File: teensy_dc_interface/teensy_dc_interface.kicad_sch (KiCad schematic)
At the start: 7 parts, among them J1 PJ301M-12, J2 PJ301M-12, J3 PJ301M-12, J4 PJ301M-12, U1 AK4458VN, U2 DEV-15583

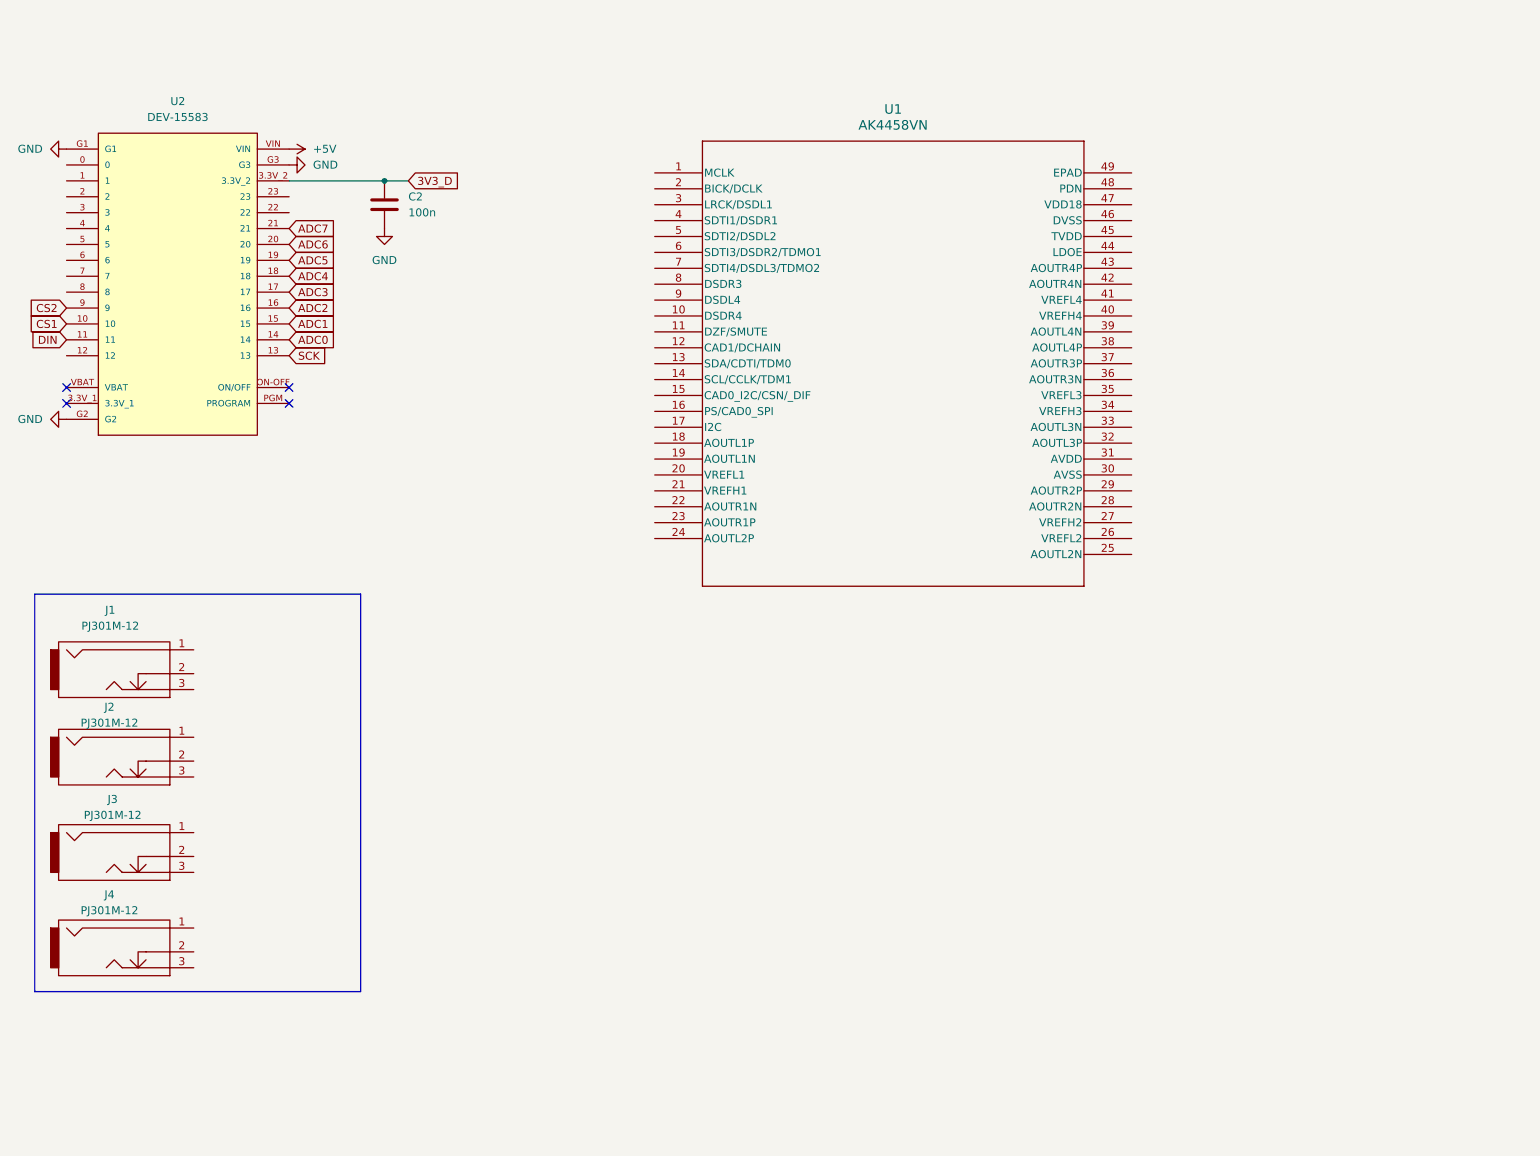
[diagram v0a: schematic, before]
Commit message: teensy interface prototype
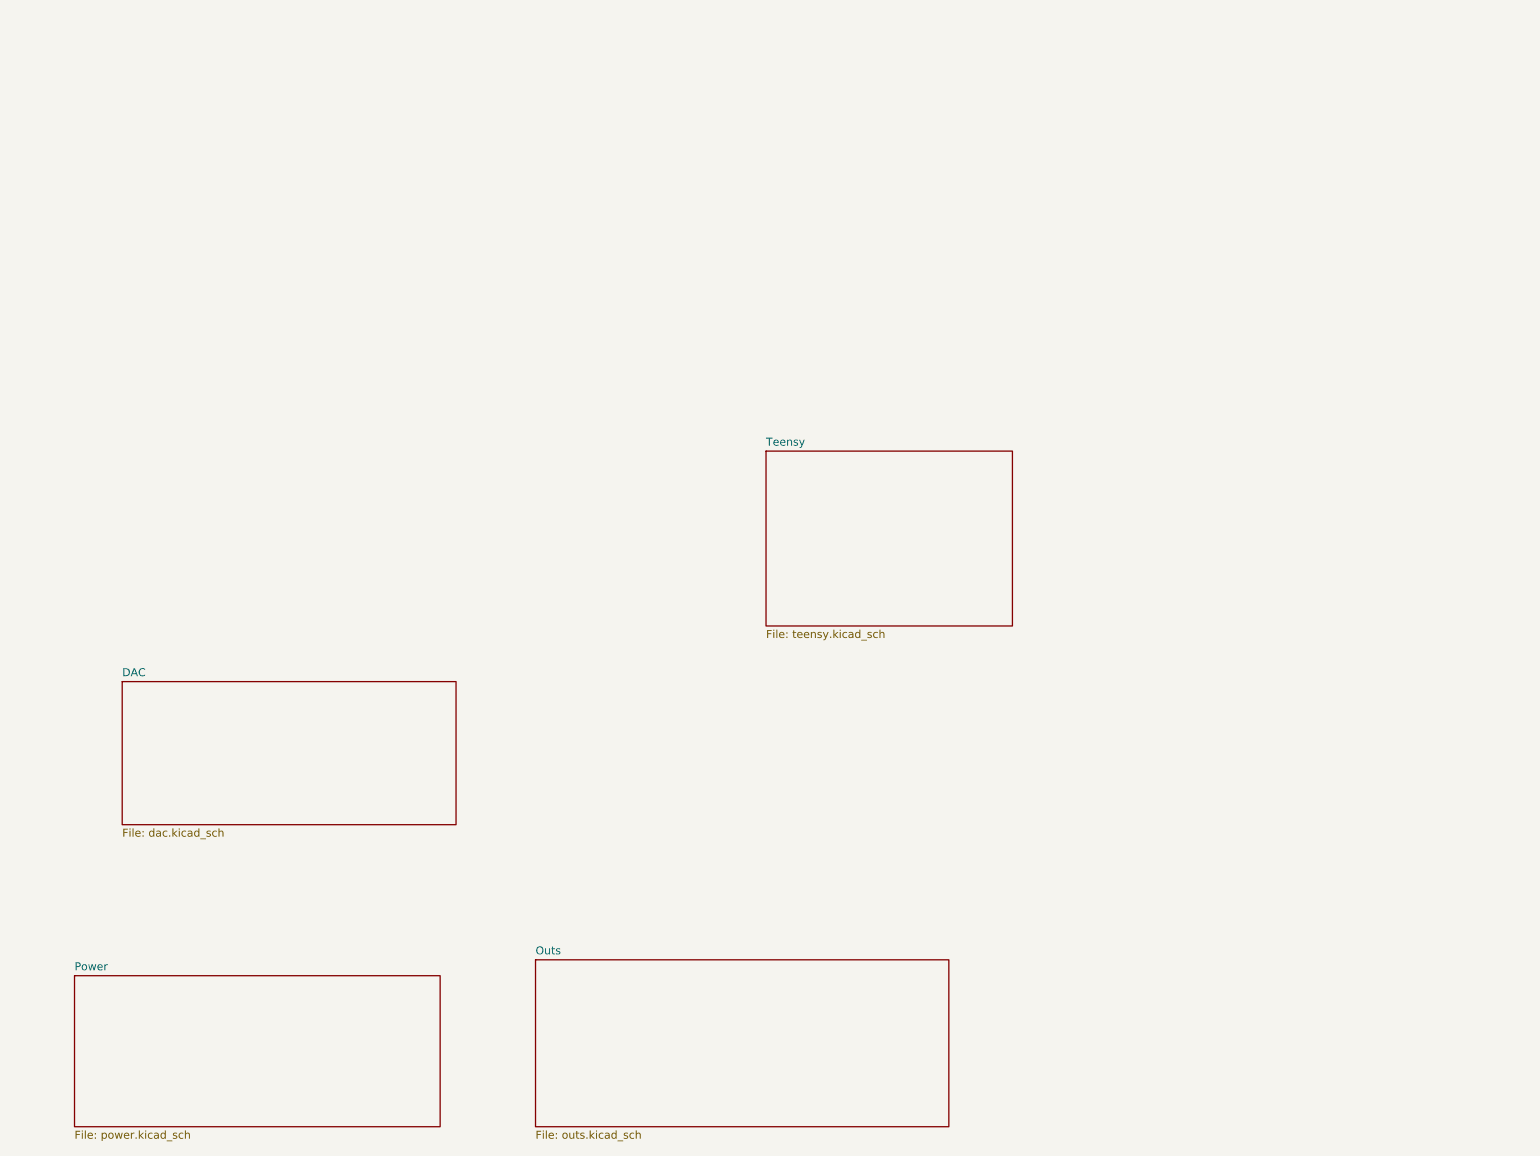
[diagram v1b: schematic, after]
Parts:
- removed C2: 100n, symbol Device:C
- removed J1, J2, J3, J4: PJ301M-12, symbol eurocad:PJ301M-12
- removed U1: AK4458VN, QFN48_7x7-0p5_AKM, symbol AK4458VN:AK4458VN
- removed U2: DEV-15583, DEV-15583:MODULE_DEV-15583, symbol Teensy4p0:DEV-15583
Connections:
- no-connect marks 4 -> 0
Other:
- added sheet DAC (dac.kicad_sch)
- added sheet Outs (outs.kicad_sch)
- added sheet Power (power.kicad_sch)
- added sheet Teensy (teensy.kicad_sch)

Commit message: teensy to dac connections
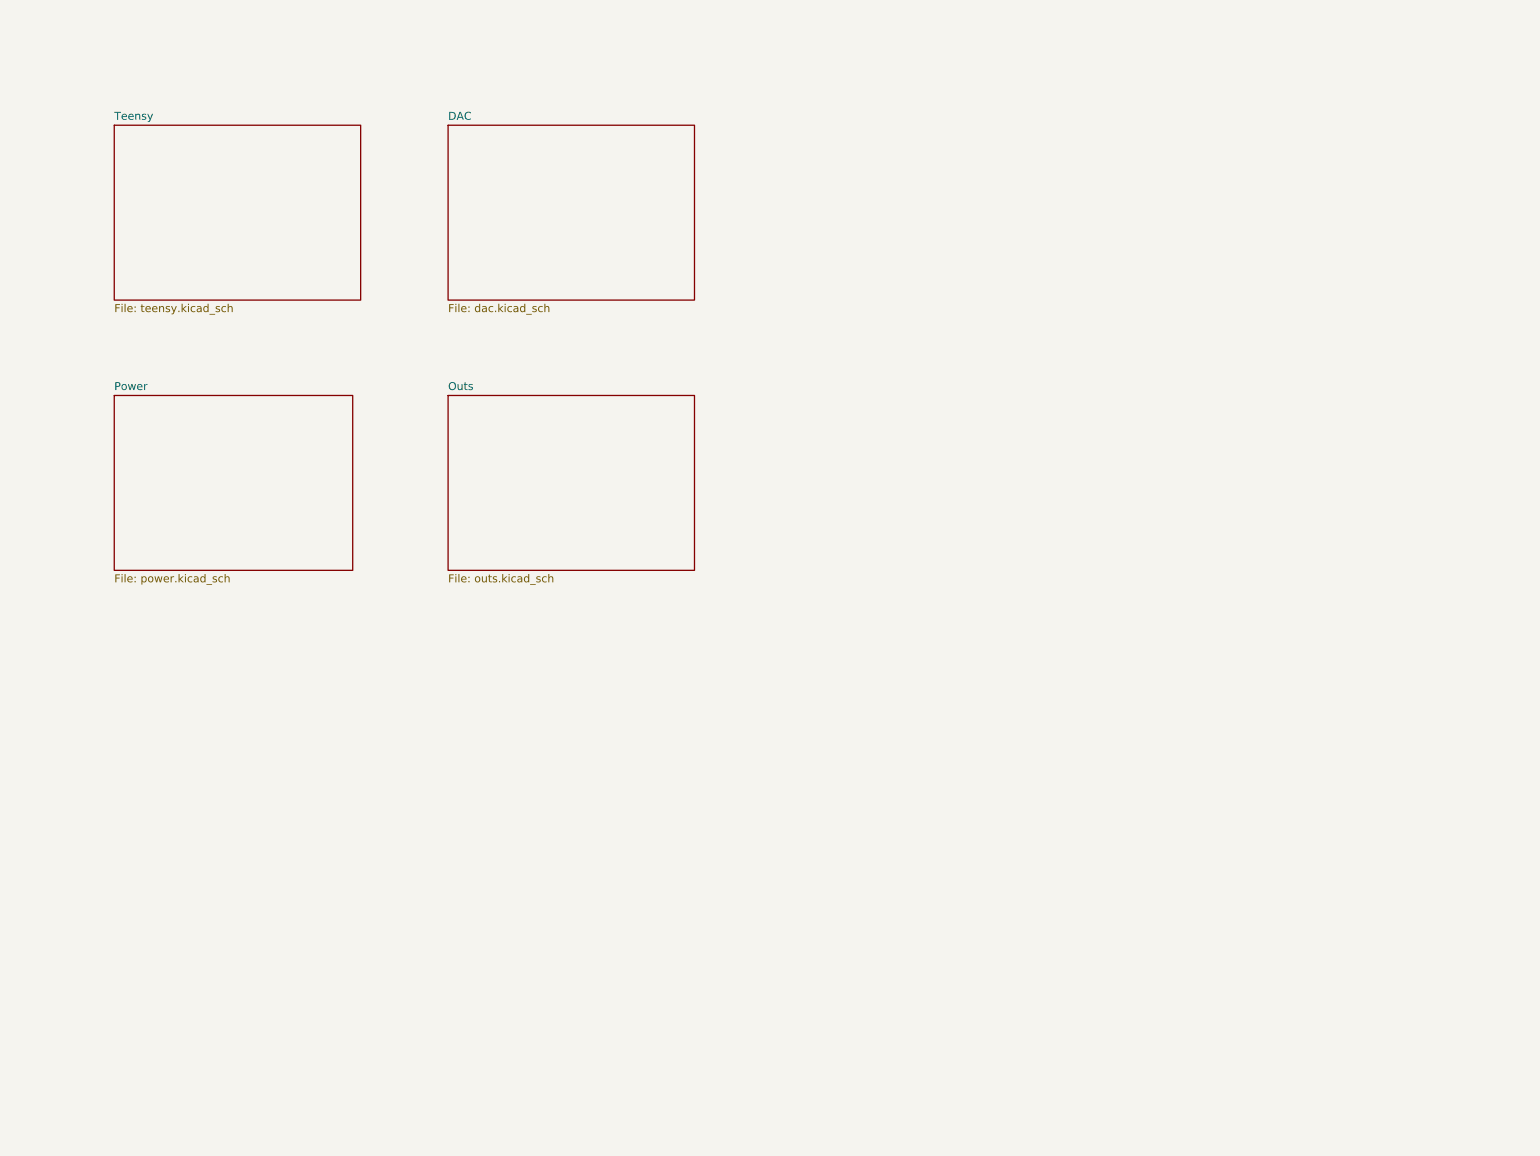
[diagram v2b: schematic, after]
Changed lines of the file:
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@@
 	(paper "A4")
 	(sheet
-		(at 20.32 166.37)
-		(size 58.42 24.13)
+		(at 26.67 73.66)
+		(size 38.1 27.94)
 		(fields_autoplaced yes)
 		(stroke
@@
 		)
 		(property "Sheetname" "Power"
-			(at 20.32 165.6584 0)
+			(at 26.67 72.9484 0)
 			(effects
 				(font
@@
 		)
 		(property "Sheetfile" "power.kicad_sch"
-			(at 20.32 191.0846 0)
+			(at 26.67 102.1846 0)
 			(effects
 				(font
@@
 	)
 	(sheet
-		(at 93.98 163.83)
-		(size 66.04 26.67)
+		(at 80.01 73.66)
+		(size 39.37 27.94)
 		(fields_autoplaced yes)
 		(stroke
@@
 		)
 		(property "Sheetname" "Outs"
-			(at 93.98 163.1184 0)
+			(at 80.01 72.9484 0)
 			(effects
 				(font
@@
 		)
 		(property "Sheetfile" "outs.kicad_sch"
-			(at 93.98 191.0846 0)
+			(at 80.01 102.1846 0)
 			(effects
 				(font
@@
 	)
 	(sheet
-		(at 27.94 119.38)
-		(size 53.34 22.86)
+		(at 80.01 30.48)
+		(size 39.37 27.94)
 		(fields_autoplaced yes)
 		(stroke
@@
 		)
 		(property "Sheetname" "DAC"
-			(at 27.94 118.6684 0)
+			(at 80.01 29.7684 0)
 			(effects
 				(font
@@
 		)
 		(property "Sheetfile" "dac.kicad_sch"
-			(at 27.94 142.8246 0)
+			(at 80.01 59.0046 0)
 			(effects
 				(font
@@
 	)
 	(sheet
-		(at 130.81 82.55)
+		(at 26.67 30.48)
 		(size 39.37 27.94)
 		(fields_autoplaced yes)
@@
 		)
 		(property "Sheetname" "Teensy"
-			(at 130.81 81.8384 0)
+			(at 26.67 29.7684 0)
 			(effects
 				(font
@@
 		)
 		(property "Sheetfile" "teensy.kicad_sch"
-			(at 130.81 111.0746 0)
+			(at 26.67 59.0046 0)
 			(effects
 				(font

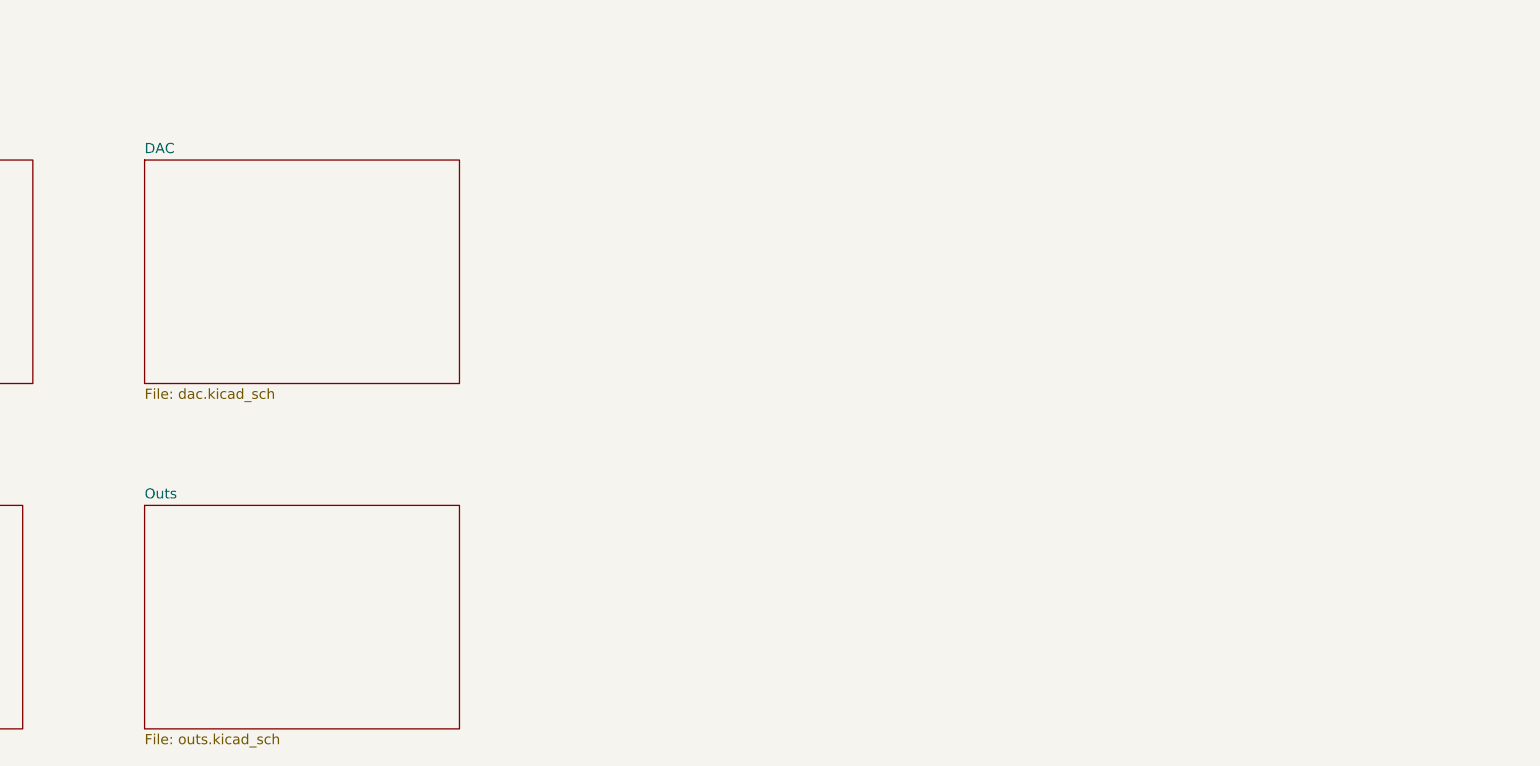
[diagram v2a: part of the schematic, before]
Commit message: out pairs as pages
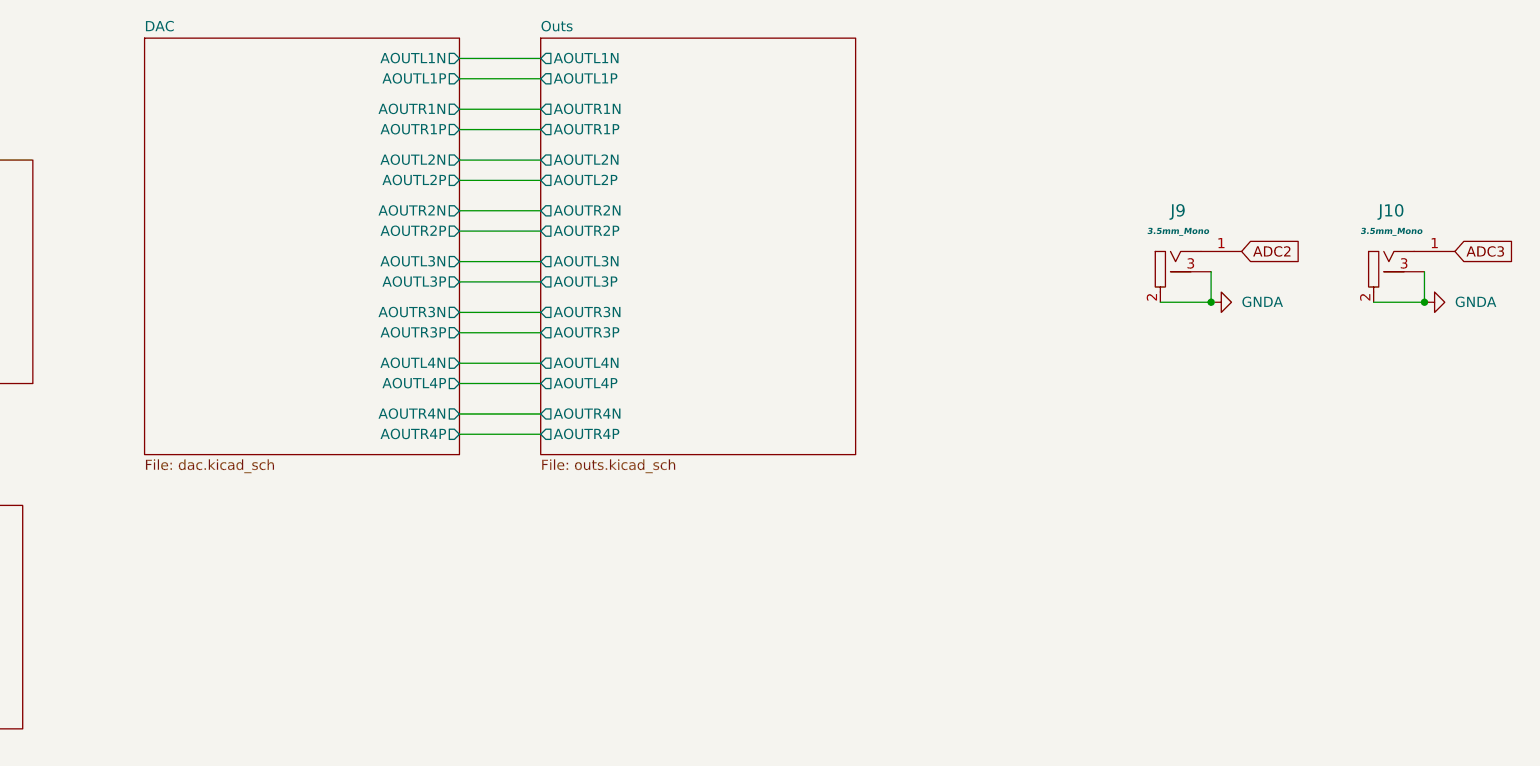
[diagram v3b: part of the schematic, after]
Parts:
- added J10, J9: 3.5mm_Mono_Switched_SymSmall_0.05, 4ms_Jack:EighthInch_PJ398SM, symbol PCM_4ms_Jack:3.5mm_Mono_Switched_SymSmall_0.05
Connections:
- new net ADC2: J9.1 (SIG)
- new net ADC3: J10.1 (SIG)
- new net GNDA: J10.2 (SHEILD), J10.3 (SW), J9.2 (SHEILD), J9.3 (SW)
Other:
- sheet DAC ports: added AOUTL1N, AOUTL1P, AOUTL2N, AOUTL2P, AOUTL3N, AOUTL3P, AOUTL4N, AOUTL4P, AOUTR1N, AOUTR1P, AOUTR2N, AOUTR2P, AOUTR3N, AOUTR3P, AOUTR4N, AOUTR4P; removed none
- sheet Outs ports: added AOUTL1N, AOUTL1P, AOUTL2N, AOUTL2P, AOUTL3N, AOUTL3P, AOUTL4N, AOUTL4P, AOUTR1N, AOUTR1P, AOUTR2N, AOUTR2P, AOUTR3N, AOUTR3P, AOUTR4N, AOUTR4P; removed none

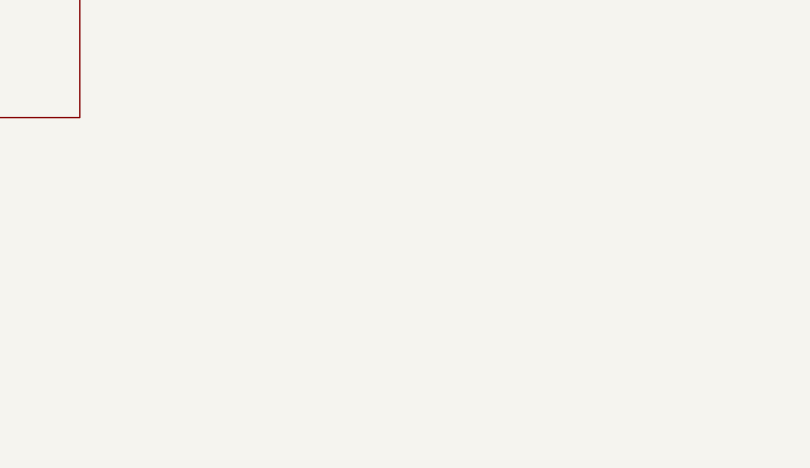
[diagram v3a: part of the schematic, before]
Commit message: mounting holes
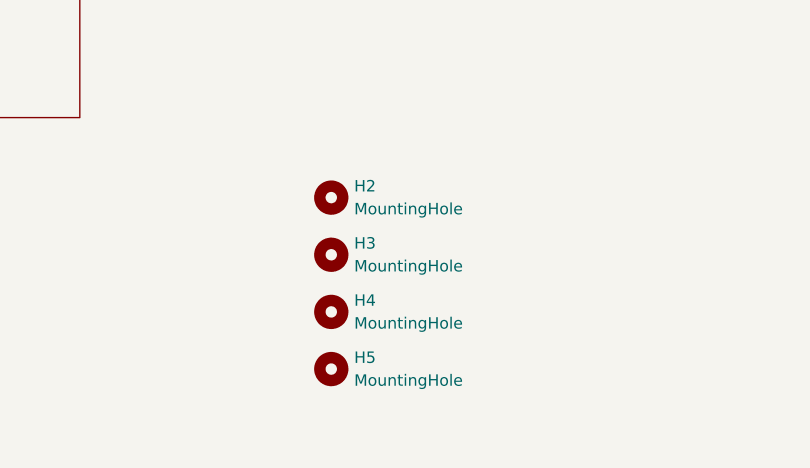
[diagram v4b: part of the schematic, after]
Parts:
- added H2, H3, H4, H5: MountingHole, 4ms_Faceplate:Faceplate_Rail_Mount_Slot_Plated, symbol Mechanical:MountingHole
